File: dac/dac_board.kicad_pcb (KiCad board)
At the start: 4 copper layers, 271.6 x 100 mm, 195 parts, among them J1 5-1814832-1, J2 5-1814832-1, J3 5-1814832-1, J4 5-1814832-1, J5 Aux power, P1 my_pcie_8x, Q1 2STD1665T4, U1 OPA2210, U101 OPA2210, U102 OPA1611, U151 PCM1794A, U17 DS90LV048, U18 74AUP1G74, U19 74AUP1G74, U201 OPA2210, U202 OPA1611, U3 OPA1611, U301 OPA2210, U302 OPA1611, U351 PCM1794A, U4 MCP1755S-3302E/DB, U401 OPA2210, U402 OPA1611, U5 NCP1117STAT3G, U6 LM337_SOT223

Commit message: DAC board is routed.  I also changed the digital interface to use a buffer (like I did on the input board) so that everything is buffered and we don't have multi-drop nets.
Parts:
- removed C73, C74: 220pF, Capacitor_SMD:C_0603_1608Metric
- removed R1, R2, R3, R4, R5, R6: 200, Resistor_SMD:R_0603_1608Metric
- removed R65, R66: 68, Resistor_SMD:R_0603_1608Metric
- added C6: 100nF, Capacitor_SMD:C_0603_1608Metric, F.Cu at (242.2, 77.5)
- added C7: 100nF, Capacitor_SMD:C_0603_1608Metric, F.Cu at (244.5, 67.8)
- added RN1: 33, Resistor_SMD:R_Array_Convex_4x0603, F.Cu at (237.8, 74.6)
- added RN2: 33, Resistor_SMD:R_Array_Convex_4x0603, F.Cu at (237.8, 69.9)
- added RN3: 33, Resistor_SMD:R_Array_Convex_4x0603, F.Cu at (250.2, 83.0)
- added TP7: VREF, TestPoint:TestPoint_Keystone_5000-5004_Miniature, F.Cu at (232.5, 123.5)
- added U2: 74LVC541A, input:my-SSOP-20_5.3x7.2mm_P0.65mm, F.Cu at (245.1, 72.6)
- J1: value 5-1814832-1 -> Out 1
- J2: value 5-1814832-1 -> Out 2
- J3: value 5-1814832-1 -> Out 3
- J4: value 5-1814832-1 -> Out 4
- moved TP6 82.2 mm to (182.0, 87.0)
- moved C22 81.1 mm to (149.2, 63.0), turned to 0 degrees
- moved C23 76.8 mm to (149.2, 138.0), turned to 0 degrees
- moved C401 67.5 mm to (142.0, 138.9), turned to 180 degrees
- moved C301 67.1 mm to (142.0, 117.0), turned to 180 degrees
- moved C102 66.4 mm to (142.0, 60.8), turned to 180 degrees
- moved C302 66.2 mm to (142.0, 103.8), turned to 180 degrees
- moved C402 65.8 mm to (142.0, 125.4), turned to 180 degrees
- moved C201 65.3 mm to (142.0, 95.8), turned to 180 degrees
- moved C101 64.1 mm to (142.0, 74.2), turned to 180 degrees
- moved C13 63.3 mm to (175.2, 63.8), turned to 0 degrees
- moved C304 59.1 mm to (144.2, 113.3)
- moved C151 58.8 mm to (170.8, 77.5)
- moved R202 57.6 mm to (139.5, 79.8)
- moved R353 57.3 mm to (165.8, 108.3), turned to 180 degrees
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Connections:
- net DOUT1+ renamed BCK+
- net DOUT1- renamed BCK-
- net DOUT2+ renamed DATA1+
- net DOUT2- renamed DATA1-
- net DOUT3+ renamed DATA2+
- net DOUT3- renamed DATA2-
- net Net-(R151-Pad2) renamed /DAC1/IREF
- net Net-(R16-Pad2) renamed /power/U3OUT
- net Net-(R351-Pad2) renamed /DAC2/IREF
- net Net-(U18-Pad2) renamed /interface/U18FB
- net Net-(U18-Pad5) renamed /interface/U18Q
- net Net-(U19-Pad2) renamed /interface/U19FB
- C101 pad 1: /DAC1/out_chan_L/IOUT+ -> /DAC1/out_chan_R/IOUT+
- C101 pad 2: /DAC1/out_chan_L/VOUT+ -> /DAC1/out_chan_R/VOUT+
- C102 pad 1: /DAC1/out_chan_L/IOUT- -> /DAC1/out_chan_R/IOUT-
- C102 pad 2: /DAC1/out_chan_L/VOUT- -> /DAC1/out_chan_R/VOUT-
- C105 pad 1: /DAC1/out_chan_L/Ux02+ -> /DAC1/out_chan_R/Ux02+
- C105 pad 2: /DAC1/OUT_REF_L -> /DAC1/OUT_REF_R
- C106 pad 1: /DAC1/out_chan_L/VOUT1 -> /DAC1/out_chan_R/VOUT1
- C106 pad 2: /DAC1/out_chan_L/Ux02- -> /DAC1/out_chan_R/Ux02-
- C109 pad 1: /DAC1/OUT_REF_L -> /DAC1/OUT_REF_R
- C201 pad 1: /DAC1/out_chan_R/IOUT+ -> /DAC1/out_chan_L/IOUT+
- C201 pad 2: /DAC1/out_chan_R/VOUT+ -> /DAC1/out_chan_L/VOUT+
- C202 pad 1: /DAC1/out_chan_R/IOUT- -> /DAC1/out_chan_L/IOUT-
- C202 pad 2: /DAC1/out_chan_R/VOUT- -> /DAC1/out_chan_L/VOUT-
- C205 pad 1: /DAC1/out_chan_R/Ux02+ -> /DAC1/out_chan_L/Ux02+
- C205 pad 2: /DAC1/OUT_REF_R -> /DAC1/OUT_REF_L
- C206 pad 1: /DAC1/out_chan_R/VOUT1 -> /DAC1/out_chan_L/VOUT1
- C206 pad 2: /DAC1/out_chan_R/Ux02- -> /DAC1/out_chan_L/Ux02-
- C209 pad 1: /DAC1/OUT_REF_R -> /DAC1/OUT_REF_L
- C301 pad 1: /DAC2/out_chan_L/IOUT+ -> /DAC2/out_chan_R/IOUT+
- C301 pad 2: /DAC2/out_chan_L/VOUT+ -> /DAC2/out_chan_R/VOUT+
- C302 pad 1: /DAC2/out_chan_L/IOUT- -> /DAC2/out_chan_R/IOUT-
- C302 pad 2: /DAC2/out_chan_L/VOUT- -> /DAC2/out_chan_R/VOUT-
- C305 pad 1: /DAC2/out_chan_L/Ux02+ -> /DAC2/out_chan_R/Ux02+
- C305 pad 2: /DAC2/OUT_REF_L -> /DAC2/OUT_REF_R
- C306 pad 1: /DAC2/out_chan_L/VOUT1 -> /DAC2/out_chan_R/VOUT1
- C306 pad 2: /DAC2/out_chan_L/Ux02- -> /DAC2/out_chan_R/Ux02-
- C309 pad 1: /DAC2/OUT_REF_L -> /DAC2/OUT_REF_R
- C401 pad 1: /DAC2/out_chan_R/IOUT+ -> /DAC2/out_chan_L/IOUT+
- C401 pad 2: /DAC2/out_chan_R/VOUT+ -> /DAC2/out_chan_L/VOUT+
- C402 pad 1: /DAC2/out_chan_R/IOUT- -> /DAC2/out_chan_L/IOUT-
- C402 pad 2: /DAC2/out_chan_R/VOUT- -> /DAC2/out_chan_L/VOUT-
- C405 pad 1: /DAC2/out_chan_R/Ux02+ -> /DAC2/out_chan_L/Ux02+
- C405 pad 2: /DAC2/OUT_REF_R -> /DAC2/OUT_REF_L
- C406 pad 1: /DAC2/out_chan_R/VOUT1 -> /DAC2/out_chan_L/VOUT1
- C406 pad 2: /DAC2/out_chan_R/Ux02- -> /DAC2/out_chan_L/Ux02-
- C409 pad 1: /DAC2/OUT_REF_R -> /DAC2/OUT_REF_L
- D101 pad 1: /DAC1/OUT_REF_L -> /DAC1/OUT_REF_R
- D101 pad 2: /DAC1/OUT_REF_L -> /DAC1/OUT_REF_R
- D102 pad 3: /DAC1/out_chan_L/VOUT2 -> /DAC1/out_chan_R/VOUT2
- D201 pad 1: /DAC1/OUT_REF_R -> /DAC1/OUT_REF_L
- D201 pad 2: /DAC1/OUT_REF_R -> /DAC1/OUT_REF_L
- D202 pad 3: /DAC1/out_chan_R/VOUT2 -> /DAC1/out_chan_L/VOUT2
- D301 pad 1: /DAC2/OUT_REF_L -> /DAC2/OUT_REF_R
- D301 pad 2: /DAC2/OUT_REF_L -> /DAC2/OUT_REF_R
- D302 pad 3: /DAC2/out_chan_L/VOUT2 -> /DAC2/out_chan_R/VOUT2
- D401 pad 1: /DAC2/OUT_REF_R -> /DAC2/OUT_REF_L
- D401 pad 2: /DAC2/OUT_REF_R -> /DAC2/OUT_REF_L
- D402 pad 3: /DAC2/out_chan_R/VOUT2 -> /DAC2/out_chan_L/VOUT2
- J1 pad 1: /DAC1/OUT_REF_L -> /DAC1/OUT_REF_R
- J1 pad 2: /DAC1/OUT_L -> /DAC1/OUT_R
- J2 pad 1: /DAC1/OUT_REF_R -> /DAC1/OUT_REF_L
- J2 pad 2: /DAC1/OUT_R -> /DAC1/OUT_L
- J3 pad 1: /DAC2/OUT_REF_L -> /DAC2/OUT_REF_R
- J3 pad 2: /DAC2/OUT_L -> /DAC2/OUT_R
- J4 pad 1: /DAC2/OUT_REF_R -> /DAC2/OUT_REF_L
- J4 pad 2: /DAC2/OUT_R -> /DAC2/OUT_L
- P1 pad A3: DOUTL1 -> ~RST_IN
- P1 pad B3: DOUTL2 -> LRCK_IN
- R101 pad 1: /DAC1/out_chan_L/VOUT+ -> /DAC1/out_chan_R/VOUT+
- R101 pad 2: /DAC1/out_chan_L/IOUT+ -> /DAC1/out_chan_R/IOUT+
- R102 pad 1: /DAC1/out_chan_L/VOUT- -> /DAC1/out_chan_R/VOUT-
- R102 pad 2: /DAC1/out_chan_L/IOUT- -> /DAC1/out_chan_R/IOUT-
- R103 pad 1: /DAC1/out_chan_L/Ux02+ -> /DAC1/out_chan_R/Ux02+
- R103 pad 2: /DAC1/out_chan_L/VOUT+ -> /DAC1/out_chan_R/VOUT+
- R104 pad 1: /DAC1/out_chan_L/Ux02- -> /DAC1/out_chan_R/Ux02-
- R104 pad 2: /DAC1/out_chan_L/VOUT- -> /DAC1/out_chan_R/VOUT-
- R105 pad 1: /DAC1/OUT_REF_L -> /DAC1/OUT_REF_R
- R105 pad 2: /DAC1/out_chan_L/Ux02+ -> /DAC1/out_chan_R/Ux02+
- R106 pad 1: /DAC1/out_chan_L/Ux02- -> /DAC1/out_chan_R/Ux02-
- R106 pad 2: /DAC1/out_chan_L/VOUT1 -> /DAC1/out_chan_R/VOUT1
- R107 pad 2: /DAC1/OUT_REF_L -> /DAC1/OUT_REF_R
- R108 pad 1: /DAC1/out_chan_L/VOUT2 -> /DAC1/out_chan_R/VOUT2
- R108 pad 2: /DAC1/out_chan_L/VOUT1 -> /DAC1/out_chan_R/VOUT1
- R109 pad 1: /DAC1/OUT_L -> /DAC1/OUT_R
- R109 pad 2: /DAC1/out_chan_L/VOUT2 -> /DAC1/out_chan_R/VOUT2
- R201 pad 1: /DAC1/out_chan_R/VOUT+ -> /DAC1/out_chan_L/VOUT+
- R201 pad 2: /DAC1/out_chan_R/IOUT+ -> /DAC1/out_chan_L/IOUT+
- R202 pad 1: /DAC1/out_chan_R/VOUT- -> /DAC1/out_chan_L/VOUT-
- R202 pad 2: /DAC1/out_chan_R/IOUT- -> /DAC1/out_chan_L/IOUT-
- R203 pad 1: /DAC1/out_chan_R/Ux02+ -> /DAC1/out_chan_L/Ux02+
- R203 pad 2: /DAC1/out_chan_R/VOUT+ -> /DAC1/out_chan_L/VOUT+
- R204 pad 1: /DAC1/out_chan_R/Ux02- -> /DAC1/out_chan_L/Ux02-
- R204 pad 2: /DAC1/out_chan_R/VOUT- -> /DAC1/out_chan_L/VOUT-
- R205 pad 1: /DAC1/OUT_REF_R -> /DAC1/OUT_REF_L
- R205 pad 2: /DAC1/out_chan_R/Ux02+ -> /DAC1/out_chan_L/Ux02+
- R206 pad 1: /DAC1/out_chan_R/Ux02- -> /DAC1/out_chan_L/Ux02-
- R206 pad 2: /DAC1/out_chan_R/VOUT1 -> /DAC1/out_chan_L/VOUT1
- R207 pad 2: /DAC1/OUT_REF_R -> /DAC1/OUT_REF_L
- R208 pad 1: /DAC1/out_chan_R/VOUT2 -> /DAC1/out_chan_L/VOUT2
- R208 pad 2: /DAC1/out_chan_R/VOUT1 -> /DAC1/out_chan_L/VOUT1
- R209 pad 1: /DAC1/OUT_R -> /DAC1/OUT_L
- R209 pad 2: /DAC1/out_chan_R/VOUT2 -> /DAC1/out_chan_L/VOUT2
- R301 pad 1: /DAC2/out_chan_L/VOUT+ -> /DAC2/out_chan_R/VOUT+
- R301 pad 2: /DAC2/out_chan_L/IOUT+ -> /DAC2/out_chan_R/IOUT+
- R302 pad 1: /DAC2/out_chan_L/VOUT- -> /DAC2/out_chan_R/VOUT-
- R302 pad 2: /DAC2/out_chan_L/IOUT- -> /DAC2/out_chan_R/IOUT-
- R303 pad 1: /DAC2/out_chan_L/Ux02+ -> /DAC2/out_chan_R/Ux02+
- R303 pad 2: /DAC2/out_chan_L/VOUT+ -> /DAC2/out_chan_R/VOUT+
- R304 pad 1: /DAC2/out_chan_L/Ux02- -> /DAC2/out_chan_R/Ux02-
- R304 pad 2: /DAC2/out_chan_L/VOUT- -> /DAC2/out_chan_R/VOUT-
- R305 pad 1: /DAC2/OUT_REF_L -> /DAC2/OUT_REF_R
- R305 pad 2: /DAC2/out_chan_L/Ux02+ -> /DAC2/out_chan_R/Ux02+
- R306 pad 1: /DAC2/out_chan_L/Ux02- -> /DAC2/out_chan_R/Ux02-
- R306 pad 2: /DAC2/out_chan_L/VOUT1 -> /DAC2/out_chan_R/VOUT1
- R307 pad 2: /DAC2/OUT_REF_L -> /DAC2/OUT_REF_R
- R308 pad 1: /DAC2/out_chan_L/VOUT2 -> /DAC2/out_chan_R/VOUT2
- R308 pad 2: /DAC2/out_chan_L/VOUT1 -> /DAC2/out_chan_R/VOUT1
- R309 pad 1: /DAC2/OUT_L -> /DAC2/OUT_R
- R309 pad 2: /DAC2/out_chan_L/VOUT2 -> /DAC2/out_chan_R/VOUT2
- R401 pad 1: /DAC2/out_chan_R/VOUT+ -> /DAC2/out_chan_L/VOUT+
- R401 pad 2: /DAC2/out_chan_R/IOUT+ -> /DAC2/out_chan_L/IOUT+
- R402 pad 1: /DAC2/out_chan_R/VOUT- -> /DAC2/out_chan_L/VOUT-
- R402 pad 2: /DAC2/out_chan_R/IOUT- -> /DAC2/out_chan_L/IOUT-
- R403 pad 1: /DAC2/out_chan_R/Ux02+ -> /DAC2/out_chan_L/Ux02+
- R403 pad 2: /DAC2/out_chan_R/VOUT+ -> /DAC2/out_chan_L/VOUT+
- R404 pad 1: /DAC2/out_chan_R/Ux02- -> /DAC2/out_chan_L/Ux02-
- R404 pad 2: /DAC2/out_chan_R/VOUT- -> /DAC2/out_chan_L/VOUT-
- R405 pad 1: /DAC2/OUT_REF_R -> /DAC2/OUT_REF_L
- R405 pad 2: /DAC2/out_chan_R/Ux02+ -> /DAC2/out_chan_L/Ux02+
- R406 pad 1: /DAC2/out_chan_R/Ux02- -> /DAC2/out_chan_L/Ux02-
- R406 pad 2: /DAC2/out_chan_R/VOUT1 -> /DAC2/out_chan_L/VOUT1
- R407 pad 2: /DAC2/OUT_REF_R -> /DAC2/OUT_REF_L
- R408 pad 1: /DAC2/out_chan_R/VOUT2 -> /DAC2/out_chan_L/VOUT2
- R408 pad 2: /DAC2/out_chan_R/VOUT1 -> /DAC2/out_chan_L/VOUT1
- R409 pad 1: /DAC2/OUT_R -> /DAC2/OUT_L
- R409 pad 2: /DAC2/out_chan_R/VOUT2 -> /DAC2/out_chan_L/VOUT2
- U101 pad 1: /DAC1/out_chan_L/VOUT+ -> /DAC1/out_chan_R/VOUT+
- U101 pad 2: /DAC1/out_chan_L/IOUT+ -> /DAC1/out_chan_R/IOUT+
- U101 pad 6: /DAC1/out_chan_L/IOUT- -> /DAC1/out_chan_R/IOUT-
- U101 pad 7: /DAC1/out_chan_L/VOUT- -> /DAC1/out_chan_R/VOUT-
- U102 pad 2: /DAC1/out_chan_L/Ux02- -> /DAC1/out_chan_R/Ux02-
- U102 pad 3: /DAC1/out_chan_L/Ux02+ -> /DAC1/out_chan_R/Ux02+
- U102 pad 6: /DAC1/out_chan_L/VOUT1 -> /DAC1/out_chan_R/VOUT1
- U17 pad 14: /interface/DATA1 -> /interface/DATA1_DRV
- U17 pad 15: /interface/DATA2 -> /interface/DATA2_DRV
- U19 pad 5: /interface/SCK -> /interface/SCK_DRV
- U201 pad 1: /DAC1/out_chan_R/VOUT+ -> /DAC1/out_chan_L/VOUT+
- U201 pad 2: /DAC1/out_chan_R/IOUT+ -> /DAC1/out_chan_L/IOUT+
- U201 pad 6: /DAC1/out_chan_R/IOUT- -> /DAC1/out_chan_L/IOUT-
- U201 pad 7: /DAC1/out_chan_R/VOUT- -> /DAC1/out_chan_L/VOUT-
- U202 pad 2: /DAC1/out_chan_R/Ux02- -> /DAC1/out_chan_L/Ux02-
- U202 pad 3: /DAC1/out_chan_R/Ux02+ -> /DAC1/out_chan_L/Ux02+
- U202 pad 6: /DAC1/out_chan_R/VOUT1 -> /DAC1/out_chan_L/VOUT1
- U301 pad 1: /DAC2/out_chan_L/VOUT+ -> /DAC2/out_chan_R/VOUT+
- U301 pad 2: /DAC2/out_chan_L/IOUT+ -> /DAC2/out_chan_R/IOUT+
- U301 pad 6: /DAC2/out_chan_L/IOUT- -> /DAC2/out_chan_R/IOUT-
- U301 pad 7: /DAC2/out_chan_L/VOUT- -> /DAC2/out_chan_R/VOUT-
- U302 pad 2: /DAC2/out_chan_L/Ux02- -> /DAC2/out_chan_R/Ux02-
- U302 pad 3: /DAC2/out_chan_L/Ux02+ -> /DAC2/out_chan_R/Ux02+
- U302 pad 6: /DAC2/out_chan_L/VOUT1 -> /DAC2/out_chan_R/VOUT1
- U351 pad 14: /DAC1/~RST -> /DAC2/~RST
- U351 pad 4: /DAC1/LRCK -> /DAC2/LRCK
- U401 pad 1: /DAC2/out_chan_R/VOUT+ -> /DAC2/out_chan_L/VOUT+
- U401 pad 2: /DAC2/out_chan_R/IOUT+ -> /DAC2/out_chan_L/IOUT+
- U401 pad 6: /DAC2/out_chan_R/IOUT- -> /DAC2/out_chan_L/IOUT-
- U401 pad 7: /DAC2/out_chan_R/VOUT- -> /DAC2/out_chan_L/VOUT-
- U402 pad 2: /DAC2/out_chan_R/Ux02- -> /DAC2/out_chan_L/Ux02-
- U402 pad 3: /DAC2/out_chan_R/Ux02+ -> /DAC2/out_chan_L/Ux02+
- U402 pad 6: /DAC2/out_chan_R/VOUT1 -> /DAC2/out_chan_L/VOUT1
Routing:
- net Earth: track 5.67 -> 428.7 mm, vias 0 -> 3
- net GND: track 0.00 -> 380.9 mm, vias 0 -> 193
- net VCOM: track 0.00 -> 205.9 mm, vias 0 -> 4
- net /DAC2/DATA: track 0.00 -> 109.4 mm, vias 0 -> 2
- net DAC_VCC: track 0.00 -> 107.5 mm, vias 0 -> 41
- net /DAC2/LRCK: track 0.00 -> 100.5 mm
- net /DAC2/SCK: track 0.00 -> 99.5 mm
- net /DAC2/BCK: track 0.00 -> 98.7 mm
- net V-: track 0.00 -> 95.6 mm, vias 0 -> 57
- net /DAC2/~RST: track 0.00 -> 94.2 mm
- net /DAC1/DATA: track 0.00 -> 89.9 mm, vias 0 -> 2
- net /power/V-_UNREG: track 0.00 -> 85.6 mm
- net V+: track 0.00 -> 81.9 mm, vias 0 -> 54
- net /DAC1/LRCK: track 0.00 -> 75.1 mm
- net /DAC1/SCK: track 0.00 -> 73.6 mm
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- added copper zone on B.Cu, net DAC_VCC
- added copper zone on In2.Cu, net DAC_VCC
- added copper zone on B.Cu, net Earth
- added copper zone on F.Cu, net Earth
- added copper zone on In1.Cu, net GND
- added copper zone on B.Cu, net V+
- added copper zone on In2.Cu, net V+
- added copper zone on B.Cu, net V-
- added copper zone on In2.Cu, net V-
- added copper zone on B.Cu, net VCC
- added copper zone on In2.Cu, net VCC
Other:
- net class Input removed
- net class Output added: clearance 0.2, trace_width 0.5, via_dia 0.6, via_drill 0.3
- net class Unused added: clearance 0.2, trace_width 0.25, via_dia 0.6, via_drill 0.3
- board text added: "Digital routing (top)"

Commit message: Everything seems ready to go for the DAC board.  Made my BOM and checked it twice. Checked footprints of new components and fixed J5, R7-R10.
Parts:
- added TP10: DATA2, TestPoint:TestPoint_THTPad_D1.5mm_Drill0.7mm, F.Cu at (238.0, 85.8)
- added TP11: SCK, TestPoint:TestPoint_THTPad_D1.5mm_Drill0.7mm, F.Cu at (226.0, 69.5)
- added TP12: LRCK, TestPoint:TestPoint_THTPad_D1.5mm_Drill0.7mm, F.Cu at (224.5, 74.2)
- added TP13: ~RST, TestPoint:TestPoint_THTPad_D1.5mm_Drill0.7mm, F.Cu at (230.5, 68.0)
- added TP8: BCK, TestPoint:TestPoint_THTPad_D1.5mm_Drill0.7mm, F.Cu at (221.0, 70.8)
- added TP9: DATA1, TestPoint:TestPoint_THTPad_D1.5mm_Drill0.7mm, F.Cu at (244.2, 83.2)
- FB1, FB2, FB3, FB4: value 21 Ohm -> 180 Ohm
- J5: footprint digikey-footprints:PinHeader_1x3_P2.54_Drill1.1mm -> input:molex_kk100_PinHeader_1x3_P2.54_Drill1.1mm
- R10, R7, R8, R9: footprint Resistor_SMD:R_0603_1608Metric -> Resistor_SMD:R_0805_2012Metric
- R11: value 7.32K -> 10K
- R12: value 6.12K -> 8.2K
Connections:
- P1 pad A48: Earth -> Net-(P1-PadA48)
- P1 pad A49: Earth -> Net-(P1-PadA49)
- P1 pad B48: Earth -> Net-(P1-PadB48)
- P1 pad B49: Earth -> Net-(P1-PadB49)
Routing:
- net Earth: track 428.7 -> 2.02 mm, vias 3 -> 0
- net VCC: vias 58 -> 74
- net V+: vias 54 -> 101
- net GND: vias 193 -> 354
- net /power/V-_UNREG: vias 0 -> 19
- added copper zone on B.Cu, net /power/V-_UNREG
- added copper zone on F.Cu, net /power/V-_UNREG
- added copper zone on F.Cu, net V+
- removed copper zone on B.Cu, net Earth
- removed copper zone on F.Cu, net Earth
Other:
- board text added: "DAC_VCC bus"
- board text added: "DAC_VCC zone"
- board text added: "I haven't connected Earth because we don't have any IO protection that uses Earth. So there is no reason to introduce that noisy net onto this board."
- board text added: "ILEMT DAC board R0 23 Oct 20"
- board text added: "K"
- board text added: "V+ bus"
- board text added: "V+ zone"
- board text added: "V- bus"
- board text added: "V- zone"
- board text added: "VCC bus"
- board text added: "VCC zone (digital)"
- board text removed: "Digital routing (top)"

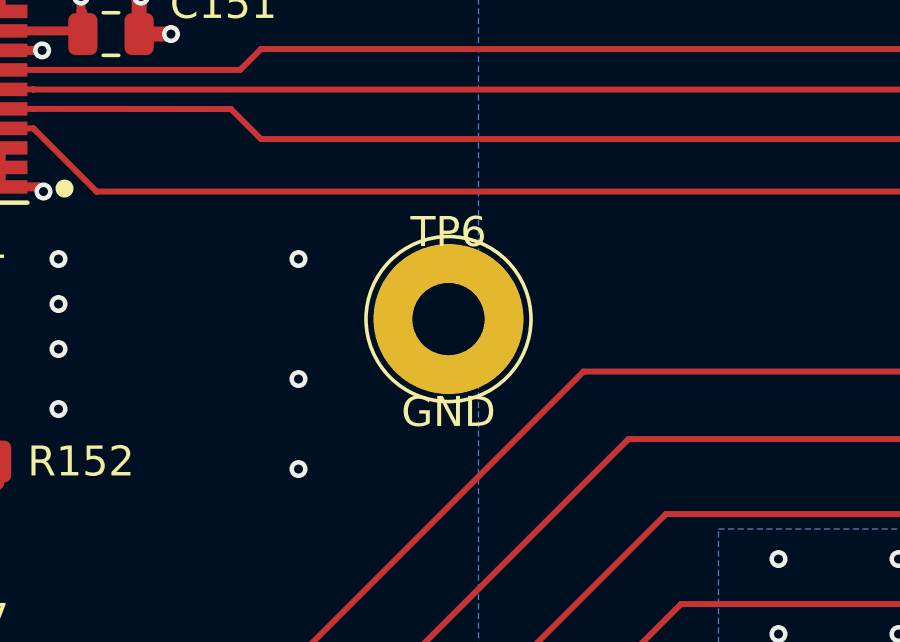
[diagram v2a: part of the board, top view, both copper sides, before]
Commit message: Mainly BOM tweaks, working on setting up more systematic database of parts and BOMs in parts/
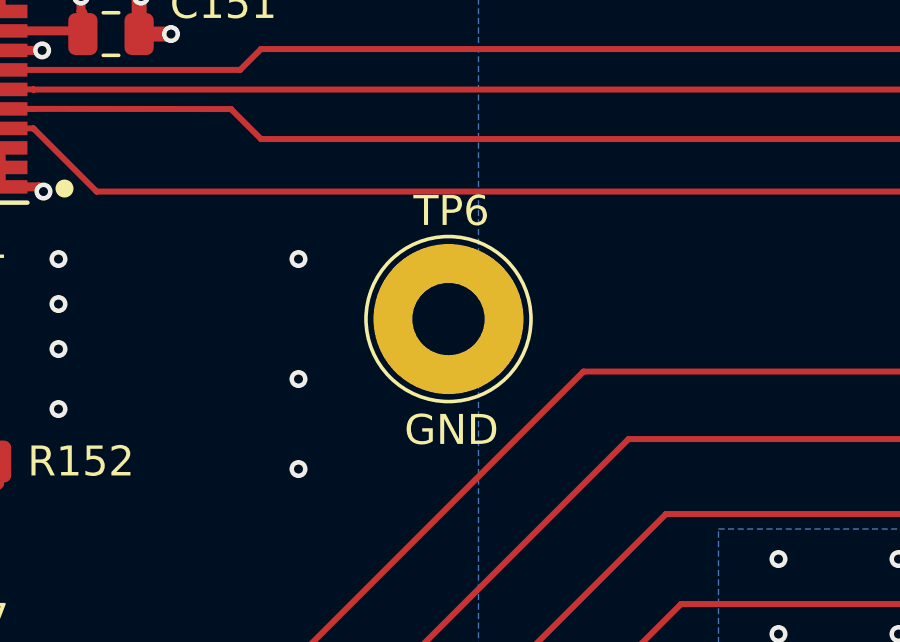
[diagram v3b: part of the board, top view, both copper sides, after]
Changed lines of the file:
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@@
       (drillshape 0)
       (scaleselection 1)
-      (outputdirectory ""))
+      (outputdirectory "output/"))
   )
   (net 0 "")
@@
     (tags "test point THT pad")
     (attr virtual)
-    (fp_text reference TP6 (at 0 -2.898) (layer F.SilkS)
-      (effects (font (size 1 1) (thickness 0.15)))
-    )
-    (fp_text value GND (at 0 3.1) (layer F.SilkS)
-      (effects (font (size 1 1) (thickness 0.15)))
-    )
+    (fp_text reference TP6 (at 0.1 -3.6) (layer F.SilkS)
+      (effects (font (size 1 1) (thickness 0.15)))
+    )
+    (fp_text value GND (at 0.1 3.7) (layer F.SilkS)
+      (effects (font (size 1 1) (thickness 0.15)))
+    )
